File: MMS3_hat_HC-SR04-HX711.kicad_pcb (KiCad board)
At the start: 2 copper layers, 100 x 50 mm, 63 parts, among them J1 Chainbus in, J10 Conn_01x04_Pin, J11 Conn_01x04_Pin, J2 Chainbus Out, J3 Conn_01x04_Pin, J4 Debug_USART_TX, J5 Conn_01x04_Pin, J6 Conn_01x04_Pin, J7 Program, J8 Conn_01x04_Pin, J9 Conn_01x04_Pin, Q3 MMBT3906, U1 SN74CB3Q3245PWR, U2 M24C64, U3 AMS1117, U5 CH32V003F4U6, U6 HX711_C6705483

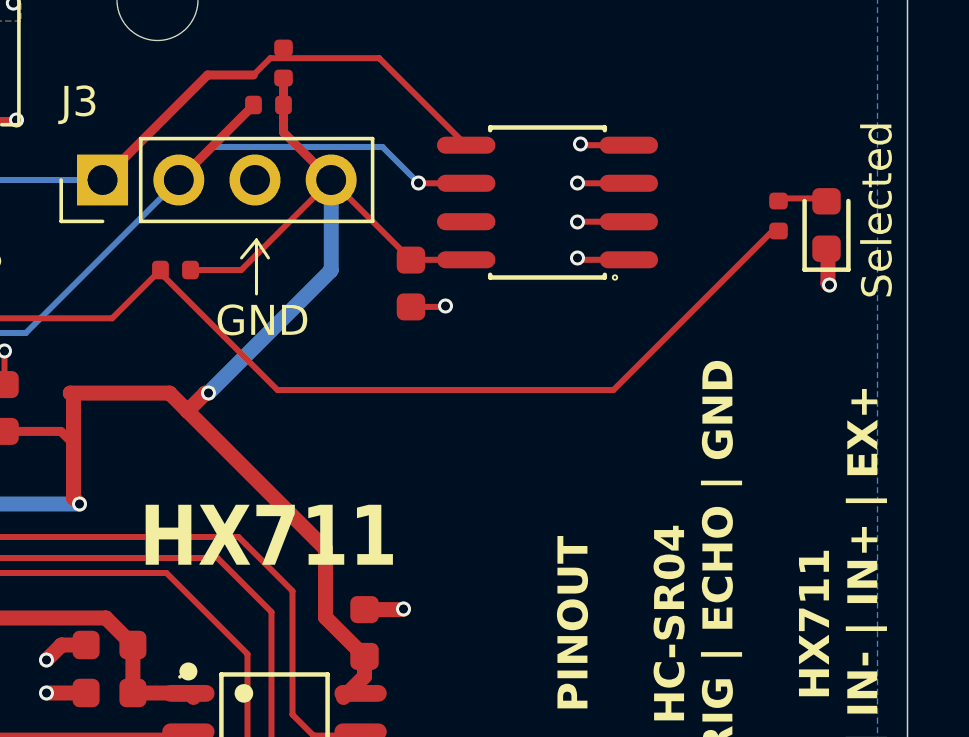
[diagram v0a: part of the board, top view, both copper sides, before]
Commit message: fixed selected led polarity
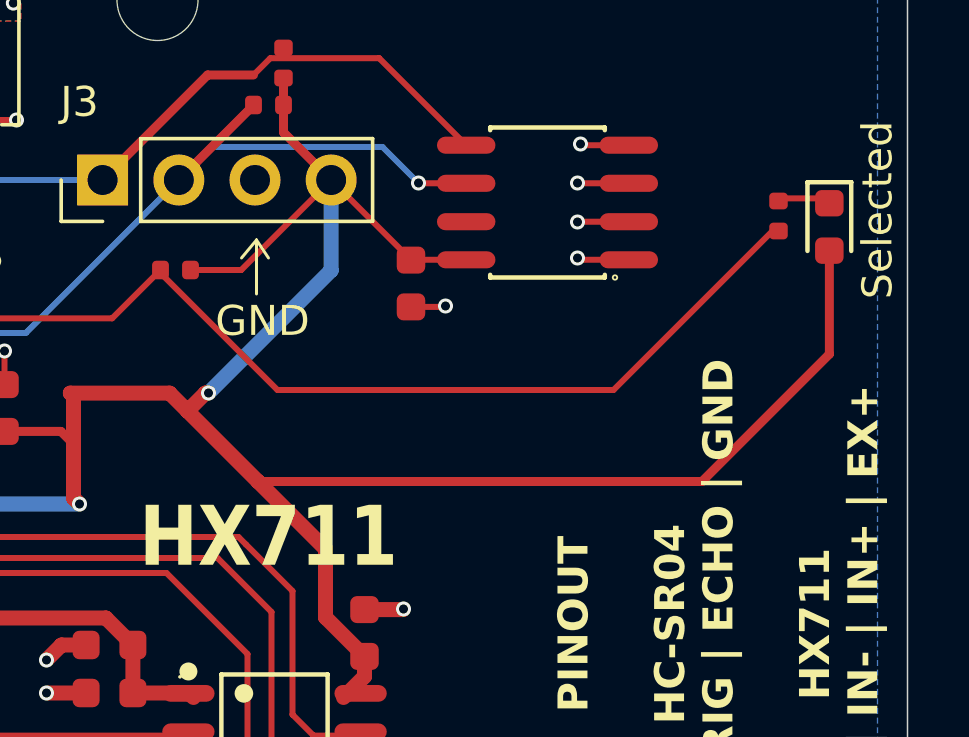
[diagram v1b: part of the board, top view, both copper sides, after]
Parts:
- moved D3 0.12 mm to (175.4, 101.6), turned to -90 degrees
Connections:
- D3 pad 1: GND -> Net-(D3-Pad1)
- D3 pad 2: Net-(D3-Pad2) -> +3V3
- R27 pad 2: Net-(D3-Pad2) -> Net-(D3-Pad1)
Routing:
- net +3V3: track 148.7 -> 173.0 mm
- net Net-(D3-Pad2): track 1.76 -> 0.00 mm
- net Net-(D3-Pad1): track 0.00 -> 1.76 mm
- net GND: track 42.4 -> 41.1 mm, vias 46 -> 45

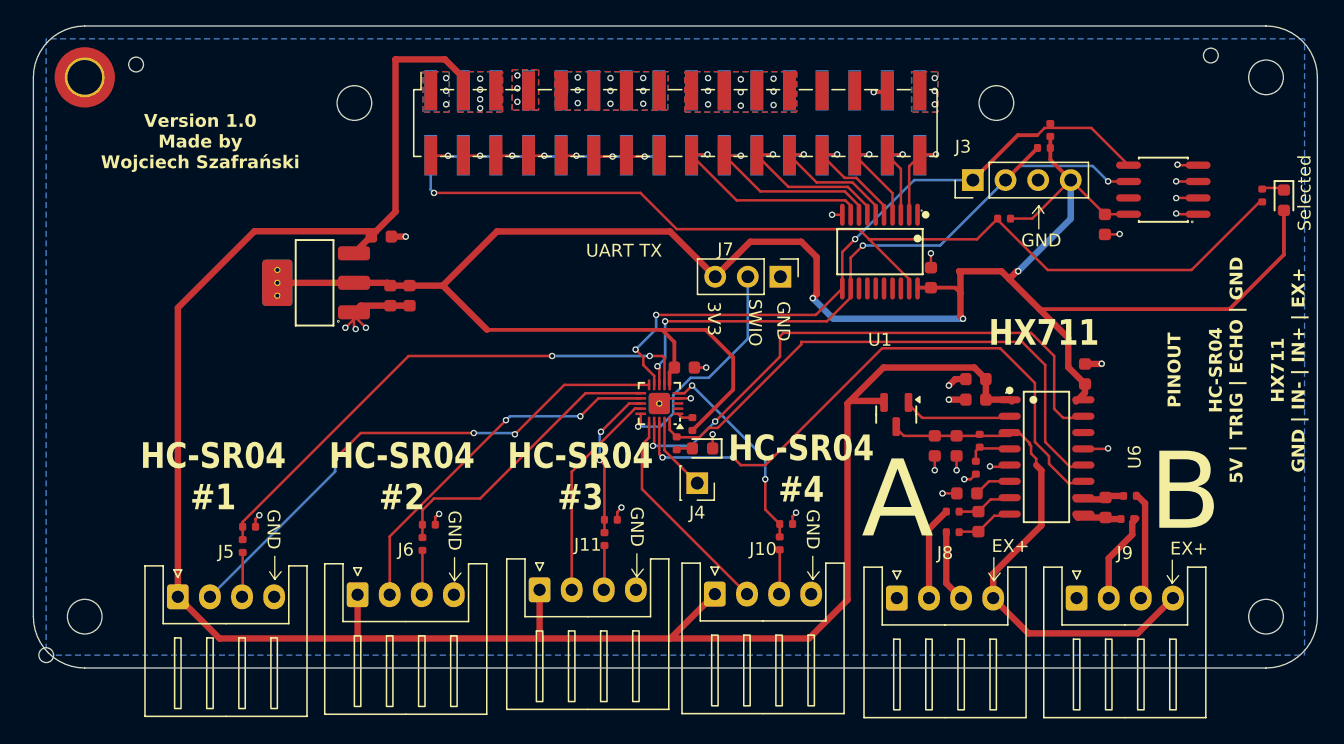
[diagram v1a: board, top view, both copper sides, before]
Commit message: made pinout on silkscreen nicer
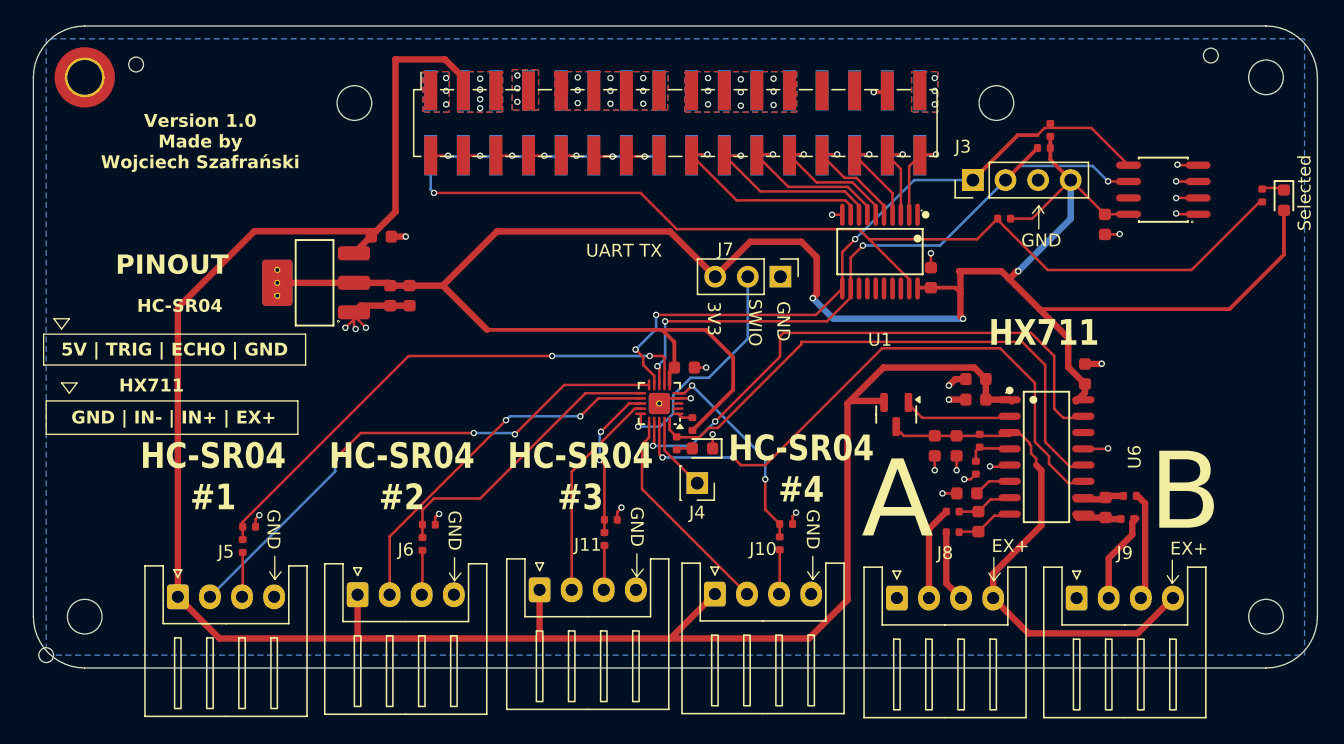
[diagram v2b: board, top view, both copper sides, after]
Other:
- board text added: "5V | TRIG | ECHO | GND"
- board text added: "GND | IN- | IN+ | EX+"
- board text added: "HC-SR04"
- board text added: "PINOUT"
- board text removed: "PINOUT HC-SR04 5V | TRIG | ECHO | GND HX711 GND | IN- | IN+ | EX+"
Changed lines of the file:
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@@
 		(embedded_fonts no)
 	)
+	(gr_rect
+		(start 78.8 112)
+		(end 99.2 114.4)
+		(stroke
+			(width 0.1)
+			(type default)
+		)
+		(fill no)
+		(layer "F.SilkS")
+	)
+	(gr_rect
+		(start 79 117.2)
+		(end 98.6 119.8)
+		(stroke
+			(width 0.1)
+			(type default)
+		)
+		(fill no)
+		(layer "F.SilkS")
+	)
+	(gr_line
+		(start 79.6 110.8)
+		(end 80.8 110.8)
+		(stroke
+			(width 0.1)
+			(type default)
+		)
+		(layer "F.SilkS")
+	)
+	(gr_line
+		(start 80.2 111.6)
+		(end 79.6 110.8)
+		(stroke
+			(width 0.1)
+			(type default)
+		)
+		(layer "F.SilkS")
+	)
+	(gr_line
+		(start 80.2 111.6)
+		(end 80.8 110.8)
+		(stroke
+			(width 0.1)
+			(type default)
+		)
+		(layer "F.SilkS")
+	)
+	(gr_line
+		(start 80.2 115.8)
+		(end 81.4 115.8)
+		(stroke
+			(width 0.1)
+			(type default)
+		)
+		(layer "F.SilkS")
+	)
+	(gr_line
+		(start 80.8 116.6)
+		(end 80.2 115.8)
+		(stroke
+			(width 0.1)
+			(type default)
+		)
+		(layer "F.SilkS")
+	)
+	(gr_line
+		(start 80.8 116.6)
+		(end 81.4 115.8)
+		(stroke
+			(width 0.1)
+			(type default)
+		)
+		(layer "F.SilkS")
+	)
 	(gr_line
 		(start 96.8 131.1)
@@
 		)
 	)
-	(gr_text "Version 1.0\nMade by\nWojciech Szafrański"
-		(at 91 97 0)
+	(gr_text "HX711"
+		(at 87.2 116 0)
 		(layer "F.SilkS")
 		(effects
@@
 		)
 	)
-	(gr_text "PINOUT\n\nHC-SR04 \n5V | TRIG | ECHO | GND\n\nHX711\nGND | IN- | IN+ | EX+"
-		(at 171.7 114.8 90)
+	(gr_text "GND | IN- | IN+ | EX+"
+		(at 88.929533 118.4931 0)
 		(layer "F.SilkS")
 		(effects
@@
 		)
 	)
+	(gr_text "5V | TRIG | ECHO | GND"
+		(at 89 113.2 0)
+		(layer "F.SilkS")
+		(effects
+			(font
+				(size 1 1)
+				(thickness 0.2)
+				(bold yes)
+			)
+		)
+	)
+	(gr_text "HC-SR04 "
+		(at 89.4 109.8 0)
+		(layer "F.SilkS")
+		(effects
+			(font
+				(size 1 1)
+				(thickness 0.2)
+				(bold yes)
+			)
+		)
+	)
+	(gr_text "Version 1.0\nMade by\nWojciech Szafrański"
+		(at 91 97 0)
+		(layer "F.SilkS")
+		(effects
+			(font
+				(size 1 1)
+				(thickness 0.2)
+				(bold yes)
+			)
+		)
+	)
+	(gr_text "PINOUT\n"
+		(at 88.8 106.6 0)
+		(layer "F.SilkS")
+		(effects
+			(font
+				(size 1.5 1.5)
+				(bold yes)
+			)
+		)
+	)
 	(gr_text "HC-SR04\n#1"
 		(at 92 123.1 0)
@@
 	)
 	(segment
+		(start 173.6125 100.6125)
+		(end 173.6 100.6)
+		(width 0.2)
+		(layer "F.Cu")
+		(net "Net-(D3-Pad1)")
+	)
+	(segment
+		(start 175.35 100.6125)
+		(end 173.6125 100.6125)
+		(width 0.2)
+		(layer "F.Cu")
+		(net "Net-(D3-Pad1)")
+	)
+	(segment
 		(start 109.072734 98.103933)
 		(end 108.994462 98.182205)
@@
 		(net "/CH32V003/PD4")
 	)
-	(segment
-		(start 173.6125 100.6125)
-		(end 173.6 100.6)
-		(width 0.2)
-		(layer "F.Cu")
-		(net "Net-(D3-Pad1)")
-	)
-	(segment
-		(start 175.35 100.6125)
-		(end 173.6125 100.6125)
-		(width 0.2)
-		(layer "F.Cu")
-		(net "Net-(D3-Pad1)")
-	)
 	(zone
